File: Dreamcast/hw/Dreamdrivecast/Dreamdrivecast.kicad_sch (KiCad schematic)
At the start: 9 parts, among them CN1 Molex_52602_0579, J1 Breakout, J2 POWER, J4 Micro_SD_Card, SW1 Lid, U1 WeAct-RP2040-Pico, U2 WeAct-RP2040-Pico

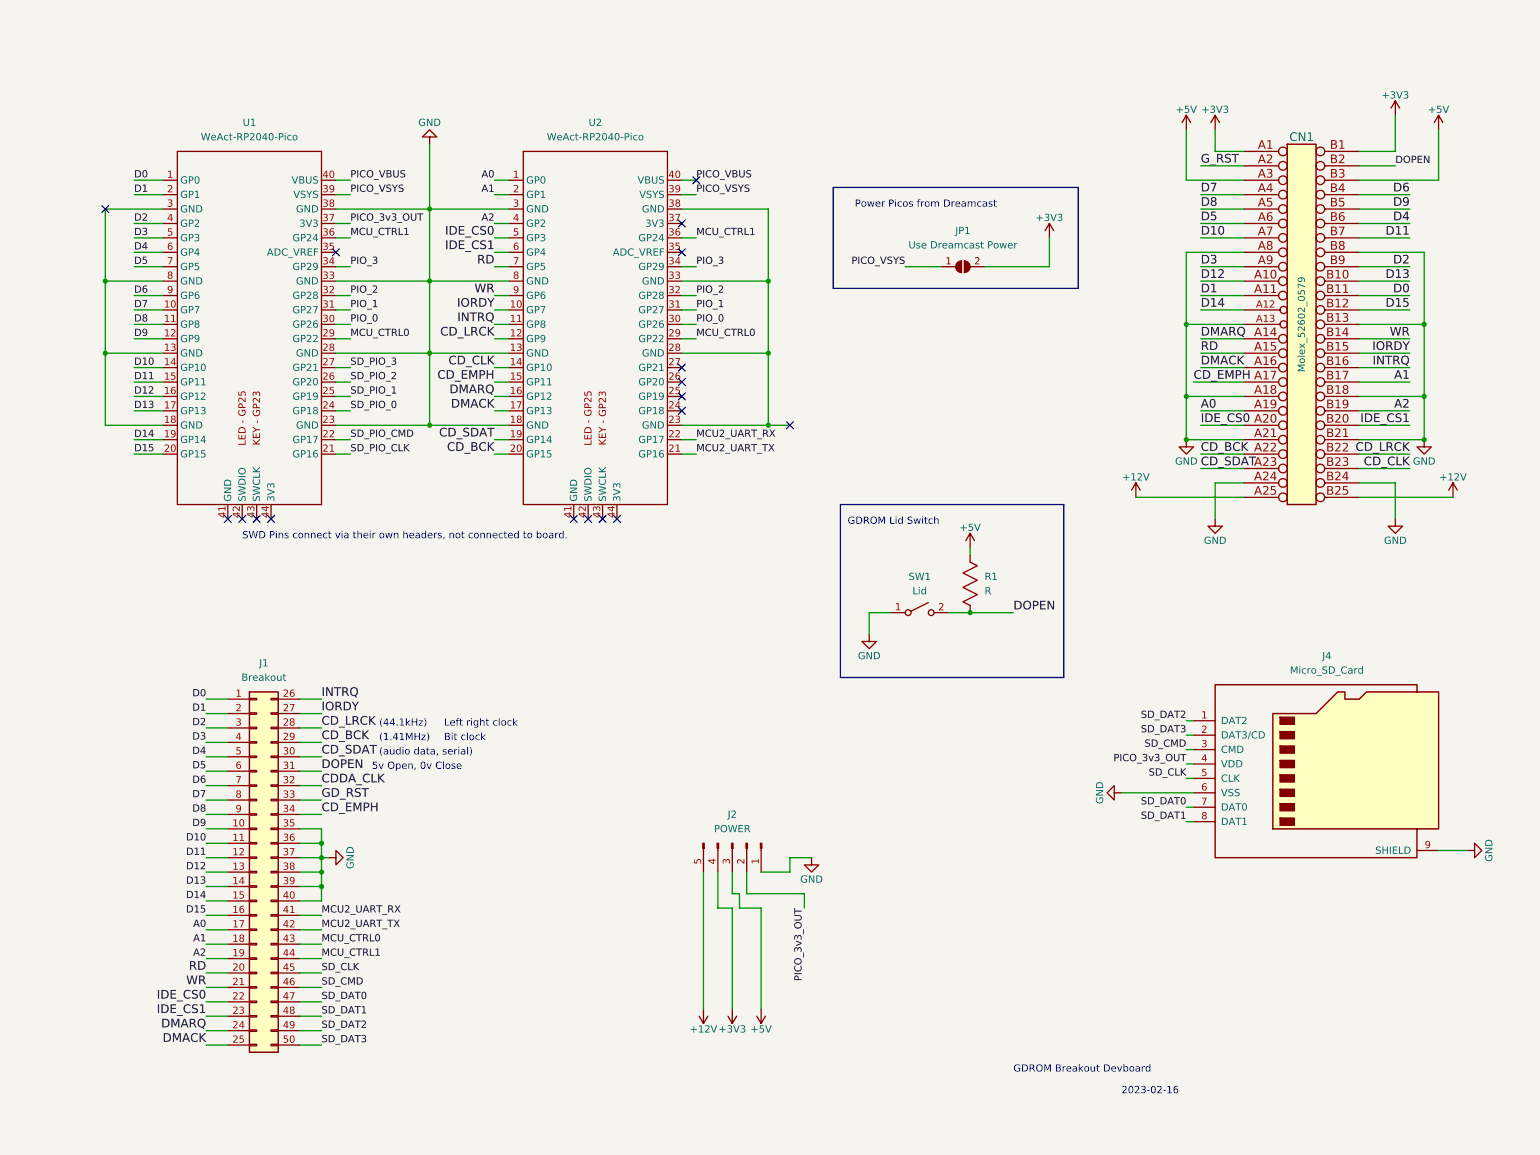
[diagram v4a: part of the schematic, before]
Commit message: Routed board, did copper fill, added silk screen for breakout, added logo and board text. Ready for fab
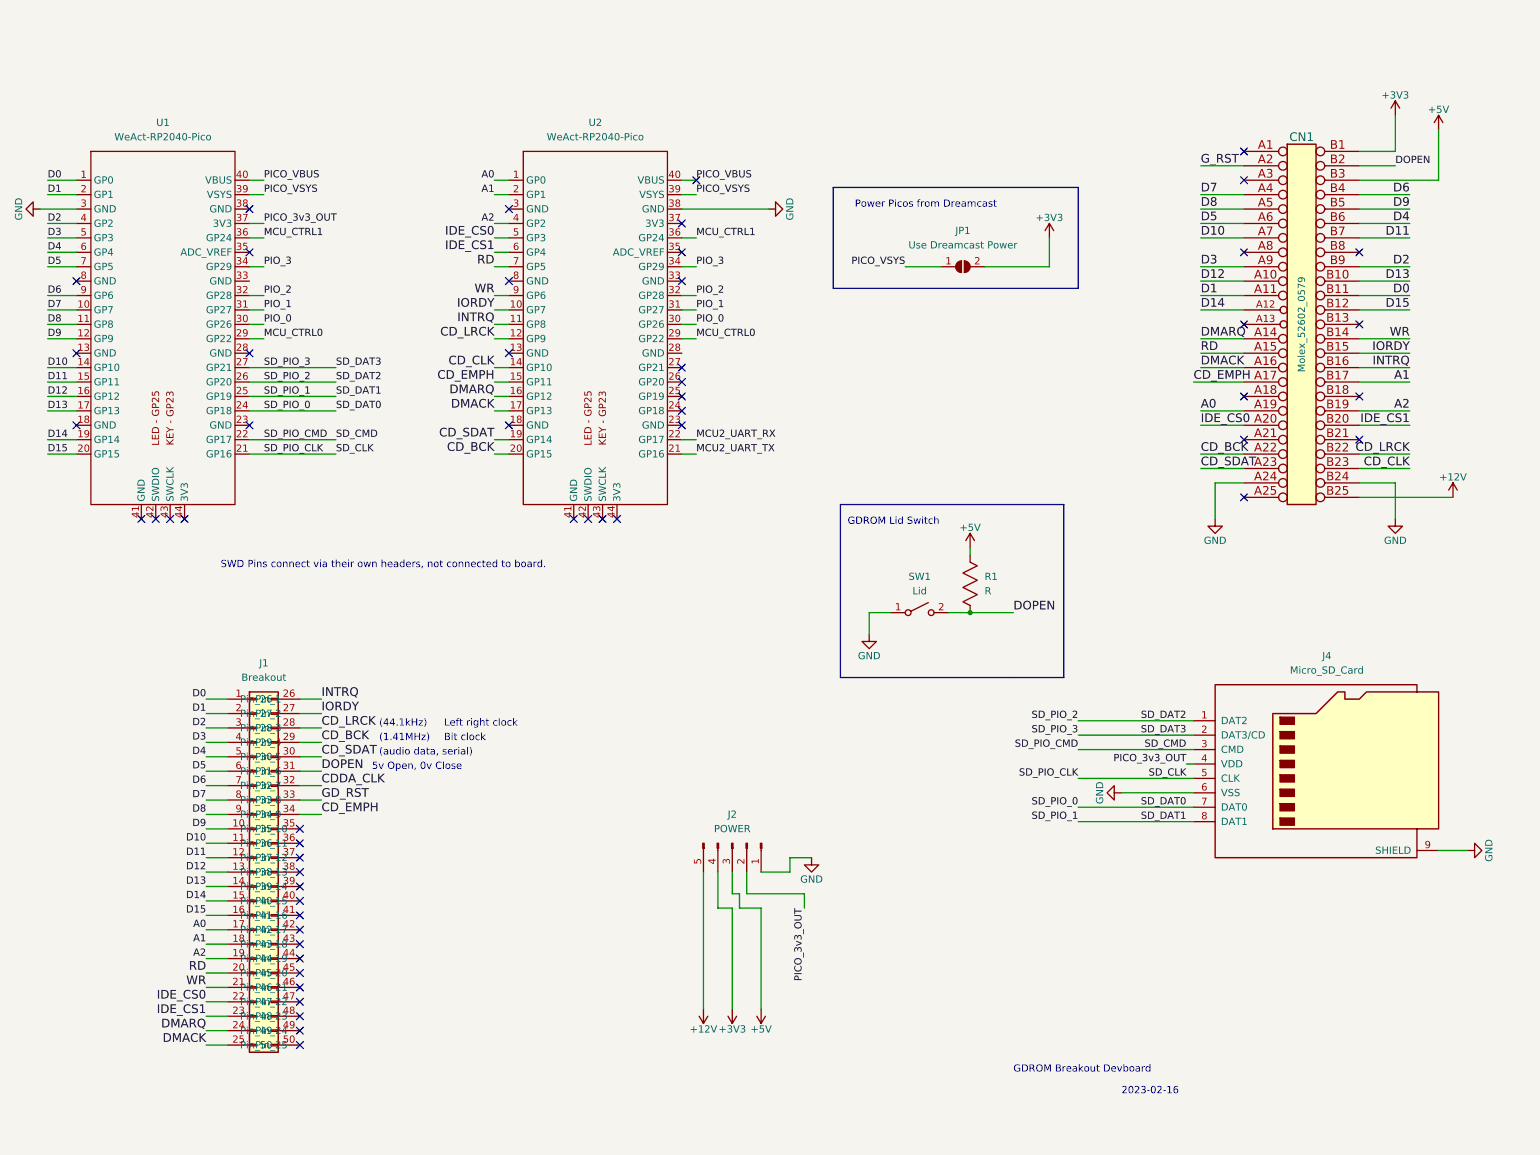
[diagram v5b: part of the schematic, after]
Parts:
- J1: footprint Connector_PinHeader_2.54mm:PinHeader_2x25_P2.54mm_Vertical_SMD -> Connector_PinHeader_2.54mm:PinHeader_2x20_P2.54mm_Vertical_SMD
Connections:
- net SD_PIO_0 is gone; now on net SD_DAT0: U1.24 (GP18)
- net SD_PIO_1 is gone; now on net SD_DAT1: U1.25 (GP19)
- net SD_PIO_2 is gone; now on net SD_DAT2: U1.26 (GP20)
- net SD_PIO_3 is gone; now on net SD_DAT3: U1.27 (GP21)
- net SD_PIO_CLK is gone; now on net SD_CLK: U1.21 (GP16)
- net SD_PIO_CMD is gone; now on net SD_CMD: U1.22 (GP17)
- net +12V: no longer CN1.A25
- net +3V3: no longer CN1.A1
- net +5V: no longer CN1.A3
- net GND: now also U1.3 (GND), U2.38 (GND); no longer CN1.A13, CN1.A18, CN1.A21, CN1.A8, CN1.B13, CN1.B18, CN1.B21, CN1.B8, J1.35 (Pin_35), J1.36 (Pin_36), J1.37 (Pin_37), J1.38 (Pin_38), J1.39 (Pin_39), J1.40 (Pin_40), U1.23 (GND), U1.28 (GND), U1.33 (GND), U1.38 (GND), U2.13 (GND), U2.18 (GND), U2.3 (GND), U2.8 (GND)
- net MCU2_UART_RX: no longer J1.41 (Pin_41)
- net MCU2_UART_TX: no longer J1.42 (Pin_42)
- net MCU_CTRL0: no longer J1.43 (Pin_43)
- net MCU_CTRL1: no longer J1.44 (Pin_44)
- net SD_CLK: no longer J1.45 (Pin_45)
- net SD_CMD: no longer J1.46 (Pin_46)
- net SD_DAT0: no longer J1.47 (Pin_47)
- net SD_DAT1: no longer J1.48 (Pin_48)
- net SD_DAT2: no longer J1.49 (Pin_49)
- net SD_DAT3: no longer J1.50 (Pin_50)
- now unconnected: U1.13 (GND), U1.18 (GND), U1.8 (GND), U2.23 (GND), U2.28 (GND), U2.33 (GND)
- no-connect marks 18 -> 55
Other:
- moved on the sheet: U1

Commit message: Update schematic to use rp2040s, mux the control lines with some data pins on mcu1, and change the pinout. PCB hasn't been rerouted yet.
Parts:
- removed J2: POWER, Connector_PinHeader_2.54mm:PinHeader_1x05_P2.54mm_Vertical, symbol Connector:Conn_01x05_Male
- removed U1, U2: WeAct-RP2040-Pico, WeAct-RP2040-Pico:WeAct-RP2040-Pico, symbol Weact-RP2040-Pico:WeAct-RP2040-Pico
- added C1, C14, C15, C16, C17, C18, C19, C2, C3, C4, C5, C6: 100n, Capacitor_SMD:C_0402_1005Metric, symbol Device:C
- added C10, C22, C23, C9: 1u, Capacitor_SMD:C_0402_1005Metric, symbol Device:C
- added C11, C12: 10u, Capacitor_SMD:C_0603_1608Metric, symbol Device:C_Small
- added C13, C24: 100n, Capacitor_SMD:C_0603_1608Metric, symbol Device:C_Small
- added C20, C21, C8: C, Capacitor_SMD:C_0402_1005Metric, symbol Device:C
- added C7: C, symbol Device:C
- added C? (x4): 12p, Capacitor_SMD:C_0402_1005Metric, symbol Device:C_Small
- added J2, J5: USB_C_Receptacle_USB2.0, Connector_USB_Extra:USB_C_Receptacle_GT-USB-7010, symbol Connector:USB_C_Receptacle_USB2.0
- added J3: POWER, Connector_PinHeader_2.54mm:PinHeader_1x05_P2.54mm_Vertical, symbol Connector:Conn_01x05_Male
- added R10, R2, R3, R9: 27.4, Resistor_SMD:R_0402_1005Metric, symbol Device:R
- added R11, R12, R4, R5: 5k1, Resistor_SMD:R_0402_1005Metric, symbol Device:R_Small
- added R13, R8: 100k, Resistor_SMD:R_0402_1005Metric, symbol Device:R_Small
- added R14, R6: 10k, Resistor_SMD:R_0402_1005Metric, symbol Device:R
- added R15, R7: 1k, Resistor_SMD:R_0402_1005Metric, symbol Device:R
- added SW2: MCU1_BOOT, symbol Switch:SW_Push
- added SW3: MCU2_BOOT, symbol Switch:SW_Push
- added U1: TS3L501ERUA, Package_DFN_QFN:WQFN-42-1EP_3.5x9mm_P0.5mm_EP2.05x7.55mm, symbol Analog_Switch:TS3L501ERUA
- added U2, U5: RP2040, Package_DFN_QFN:QFN-56-1EP_7x7mm_P0.4mm_EP3.2x3.2mm, symbol MCU_RaspberryPi:RP2040
- added U3: AZ1117-3.3, Package_TO_SOT_SMD:SOT-223, symbol Regulator_Linear:AZ1117-3.3
- added U4, U6: W25Q128JVS, Package_SO:SOIC-8_5.23x5.23mm_P1.27mm, symbol Memory_Flash:W25Q128JVS
- added Y? (x2): 12MHz 10ppm, Crystal:Crystal_SMD_2520-4Pin_2.5x2.0mm, symbol Device:Crystal_GND24_Small
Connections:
- net +12V: now also CN1.A25, J3.5 (Pin_5)
- net +3V3: now also C1.1, C10.1, C12.1, C13.1, C14.1, C15.1, C16.1, C17.1, C18.1, C19.1, C2.1, C23.1, C24.1, C3.1, C4.1, C5.1, C6.1, J3.4 (Pin_4), R14.1, R6.1, U1.1 (VDD), U1.14 (VDD), U1.21 (VDD), U1.30 (VDD), U1.39 (VDD), U1.4 (VDD), U1.8 (VDD), U2.1 (IOVDD), U2.10 (IOVDD), U2.22 (IOVDD), U2.33 (IOVDD), U2.42 (IOVDD), U2.43 (ADC_AVDD), U2.44 (VREG_IN), U2.48 (USB_VDD), U2.49 (IOVDD), U3.2 (VO), U4.8 (VCC), U5.1 (IOVDD), U5.10 (IOVDD), U5.22 (IOVDD), U5.33 (IOVDD), U5.42 (IOVDD), U5.43 (ADC_AVDD), U5.44 (VREG_IN), U5.48 (USB_VDD), U5.49 (IOVDD), U6.8 (VCC); no longer CN1.B1, JP1.2 (B)
- net +5V: now also CN1.A3, J3.3 (Pin_3)
- net A0: now also U1.38 (B0)
- net A1: now also U1.37 (B1)
- net A2: now also U1.34 (B2)
- net CD_BCK: now also U5.4 (GPIO2)
- net CD_CLK: now also U5.2 (GPIO0)
- net CD_EMPH: now also U5.6 (GPIO4)
- net CD_LRCK: now also U5.3 (GPIO1)
- net CD_SDAT: now also U5.5 (GPIO3)
- net D0: now also U1.36 (C0)
- net D1: now also U1.35 (C1)
- net D10: now also U2.13 (GPIO10)
- net D11: now also U2.14 (GPIO11)
- net D12: now also U2.15 (GPIO12)
- net D13: now also U2.16 (GPIO13)
- net D14: now also U2.17 (GPIO14)
- net D15: now also U2.18 (GPIO15)
- net D2: now also U1.32 (C2)
- net D3: now also U1.31 (C3)
- net D4: now also U1.27 (C4)
- net D5: now also U2.7 (GPIO5)
- net D6: now also U2.8 (GPIO6)
- net D7: now also U2.9 (GPIO7)
- net D8: now also U2.11 (GPIO8)
- net D9: now also U2.12 (GPIO9)
- net DMACK: now also U2.30 (GPIO19)
- net DMARQ: now also U2.31 (GPIO20)
- net GND: now also CN1.A13, CN1.A18, CN1.A21, CN1.A8, CN1.B13, CN1.B18, CN1.B21, CN1.B8, C1.2, C10.2, C11.2, C12.2, C13.2, C14.2, C15.2, C16.2, C17.2, C18.2, C19.2, C2.2, C20.2, C21.2, C22.2, C23.2, C24.2, C3.2, C4.2, C5.2, C6.2, C7.2, C8.2, C9.2, C?.1, C?.1, C?.1, C?.1, J2.A1 (GND), J2.A12 (GND), J2.B1 (GND), J2.B12 (GND), J3.1 (Pin_1), J5.A1 (GND), J5.A12 (GND), J5.B1 (GND), J5.B12 (GND), R11.2, R12.2, R13.1, R4.2, R5.2, R8.1, SW2.1, SW3.1, U1.43 (GND), U1.5 (PD), U2.19 (TESTEN), U2.57 (GND), U3.1 (GND), U4.4 (GND), U5.19 (TESTEN), U5.57 (GND), U6.4 (GND), Y?.2, Y?.2, Y?.4, Y?.4
- net INTRQ: now also U2.29 (GPIO18)
- net IORDY: now also U5.18 (GPIO15)
- net PICO_3v3_OUT: now also J3.2 (Pin_2)
- net +3V3_DREAMCAST: now reaches CN1.A1
- net +3V3_DREAMCAST: now also CN1.B1, JP1.2 (B)
- net RD renamed MCU1_GPIO16
- net MCU1_GPIO16: now also U2.27 (GPIO16)
- net SD_CLK renamed MCU1_GPIO21
- net MCU1_GPIO21: now also U2.32 (GPIO21)
- net SD_CMD renamed MCU1_GPIO22
- net MCU1_GPIO22: now also U2.34 (GPIO22)
- net SD_DAT0 renamed MCU1_GPIO23
- net MCU1_GPIO23: now also U2.35 (GPIO23)
- net SD_DAT1 renamed MCU1_GPIO24
- net MCU1_GPIO24: now also U2.36 (GPIO24)
- net SD_DAT2 renamed MCU1_GPIO25
- net MCU1_GPIO25: now also U2.37 (GPIO25)
- net SD_DAT3 renamed MCU1_GPIO26
- net MCU1_GPIO26: now also U2.38 (GPIO26_ADC0)
- net WR renamed MCU1_GPIO17
- net MCU1_GPIO17: now also U2.28 (GPIO17)
- new net: J2.B5 (CC2), R5.1
- new net: R2.2, U2.47 (USB_DP)
- new net: J5.A4 (VBUS), J5.A9 (VBUS), J5.B4 (VBUS), J5.B9 (VBUS)
- new net: J5.A5 (CC1), R11.1
- new net: J5.B5 (CC2), R12.1
- new net: J5.S1 (SHIELD), R13.2
- new net: R3.2, U2.46 (USB_DM)
- new net: J2.A5 (CC1), R4.1
- new net: R7.1, SW2.2
- new net: J2.S1 (SHIELD), R8.2
- new net: R15.1, SW3.2
- new net: R10.2, U5.46 (USB_DM)
- new net: R9.2, U5.47 (USB_DP)
- new net +1V1: C20.1, C21.1, C22.1, C7.1, C8.1, C9.1, U2.23 (DVDD), U2.45 (VREG_VOUT), U2.50 (DVDD), U5.23 (DVDD), U5.45 (VREG_VOUT), U5.50 (DVDD)
- new net COMMS_PIO_0: U2.40 (GPIO28_ADC2), U5.7 (GPIO5)
- new net COMMS_PIO_1: U2.41 (GPIO29_ADC3), U5.8 (GPIO6)
- new net CS0: U1.33 (B3)
- new net CS1: U1.29 (B4)
- new net MCU1_GPIO0: U1.2 (A0), U2.2 (GPIO0)
- new net MCU1_GPIO1: U1.3 (A1), U2.3 (GPIO1)
- new net MCU1_GPIO2: U1.6 (A2), U2.4 (GPIO2)
- new net MCU1_GPIO27: U1.13 (SEL), U2.39 (GPIO27_ADC1)
- new net MCU1_GPIO3: U1.7 (A3), U2.5 (GPIO3)
- new net MCU1_GPIO4: U1.9 (A4), U2.6 (GPIO4)
- new net MCU1_QSPI_SCLK: U2.52 (QSPI_SCLK), U4.6 (CLK)
- new net MCU1_QSPI_SD0: U2.53 (QSPI_SD0), U4.5 (DI(IO0))
- new net MCU1_QSPI_SD1: U2.55 (QSPI_SD1), U4.2 (DO(IO1))
- new net MCU1_QSPI_SD2: U2.54 (QSPI_SD2), U4.3 (IO2)
- new net MCU1_QSPI_SD3: U2.51 (QSPI_SD3), U4.7 (IO3)
- new net MCU1_QSPI_SS: R6.2, R7.2, U2.56 (QSPI_SS), U4.1 (~{CS})
- new net MCU1_RUN: U2.26 (RUN), U5.26 (RUN)
- new net MCU1_SWCLK: U2.24 (SWCLK)
- new net MCU1_SWD: U2.25 (SWD)
- new net MCU1_USB_D+: J2.A6 (D+), J2.B6 (D+), R2.1
- new net MCU1_USB_D-: J2.A7 (D-), J2.B7 (D-), R3.1
- new net MCU1_XIN: C?.2, U2.20 (XIN), Y?.3
- new net MCU1_XOUT: C?.2, U2.21 (XOUT), Y?.1
- new net MCU2_GPIO10: U5.13 (GPIO10)
- new net MCU2_GPIO11: U5.14 (GPIO11)
- new net MCU2_GPIO12: U5.15 (GPIO12)
- new net MCU2_GPIO13: U5.16 (GPIO13)
- new net MCU2_GPIO14: U5.17 (GPIO14)
- new net MCU2_GPIO16: U5.27 (GPIO16)
- new net MCU2_GPIO17: U5.28 (GPIO17)
- new net MCU2_GPIO18: U5.29 (GPIO18)
- new net MCU2_GPIO19: U5.30 (GPIO19)
- new net MCU2_GPIO20: U5.31 (GPIO20)
- new net MCU2_GPIO21: U5.32 (GPIO21)
- new net MCU2_GPIO22: U5.34 (GPIO22)
- new net MCU2_GPIO23: U5.35 (GPIO23)
- new net MCU2_GPIO24: U5.36 (GPIO24)
- new net MCU2_GPIO25: U5.37 (GPIO25)
- new net MCU2_GPIO26: U5.38 (GPIO26_ADC0)
- new net MCU2_GPIO27: U5.39 (GPIO27_ADC1)
- new net MCU2_GPIO28: U5.40 (GPIO28_ADC2)
- new net MCU2_GPIO29: U5.41 (GPIO29_ADC3)
- new net MCU2_GPIO7: U5.9 (GPIO7)
- new net MCU2_GPIO8: U5.11 (GPIO8)
- new net MCU2_GPIO9: U5.12 (GPIO9)
- new net MCU2_QSPI_SCLK: U5.52 (QSPI_SCLK), U6.6 (CLK)
- new net MCU2_QSPI_SD0: U5.53 (QSPI_SD0), U6.5 (DI(IO0))
- new net MCU2_QSPI_SD1: U5.55 (QSPI_SD1), U6.2 (DO(IO1))
- new net MCU2_QSPI_SD2: U5.54 (QSPI_SD2), U6.3 (IO2)
- new net MCU2_QSPI_SD3: U5.51 (QSPI_SD3), U6.7 (IO3)
- new net MCU2_QSPI_SS: R14.2, R15.2, U5.56 (QSPI_SS), U6.1 (~{CS})
- new net MCU2_SWCLK: U5.24 (SWCLK)
- new net MCU2_SWD: U5.25 (SWD)
- new net MCU2_USB_D+: J5.A6 (D+), J5.B6 (D+), R9.1
- new net MCU2_USB_D-: J5.A7 (D-), J5.B7 (D-), R10.1
- new net MCU2_XIN: C?.2, U5.20 (XIN), Y?.3
- new net MCU2_XOUT: C?.2, U5.21 (XOUT), Y?.1
- new net MUX_B_5: U1.28 (B5)
- new net MUX_B_6: U1.25 (B6)
- new net MUX_B_7: U1.24 (B7)
- new net MUX_COMMON_5: U1.10 (A5)
- new net MUX_COMMON_6: U1.11 (A6)
- new net MUX_COMMON_7: U1.12 (A7)
- new net MUX_C_5: U1.26 (C5)
- new net MUX_C_6: U1.23 (C6)
- new net MUX_C_7: U1.22 (C7)
- new net VBUS: C11.1, J2.A4 (VBUS), J2.A9 (VBUS), J2.B4 (VBUS), J2.B9 (VBUS), U3.3 (VI)
- no-connect marks 55 -> 29
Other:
- note added: "2023-04-20"
- note added: "AICA Chip Clock"
- note added: "Asserted in PIO mode, Deasserted in DMA mode"
- note added: "Breakouts"
- note added: "Crystals"
- note added: "DREAMCAST"
- note added: "GDROM DEV BOARD"
- note added: "IORDY - Used to signal to host that device needs more time"
- note added: "MCU1"
- note added: "MCU1 Connections"
- note added: "MCU1 Flash"
- note added: "MCU1 MUX"
- note added: "MCU1 USB connector"
- note added: "MCU2"
- note added: "MCU2 Connections"
- note added: "MCU2 Flash"
- note added: "MCU2 USB connector"
- note added: "Reset the GDROM Drive?"
- note added: "SD Card"
- note added: "USE MCU1's POWER???"
- note added: "Unused for the moment"
- note removed: "2023-02-16"
- note removed: "GDROM Breakout Devboard"
- note removed: "SWD Pins connect via their own headers, not connected to board."
- moved on the sheet: CN1, J1, J4, JP1, R1, SW1

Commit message: Updated PCB for new schematic design, still needs to be routed.
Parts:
- C11, C12, C13, C24: footprint Capacitor_SMD:C_0603_1608Metric -> Capacitor_SMD:C_0402_1005Metric
- C20, C21, C7, C8: value C -> 100n
- J1: now left out of the parts list
- J3: renamed from J2; footprint Connector_USB_Extra:USB_C_Receptacle_GT-USB-7010 -> Connector_USB:USB_C_Receptacle_Palconn_UTC16-G
- J4: renamed from J5; footprint Connector_USB_Extra:USB_C_Receptacle_GT-USB-7010 -> Connector_USB:USB_C_Receptacle_Palconn_UTC16-G
- SW2, SW3: footprint (none) -> Button_Switch_SMD:SW_SPST_FSMSM
- gave numbers to parts that had none: 6
- renumbered J3 to J2, J4 to J5
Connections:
- net PICO_VSYS is gone; now on net VBUS: JP1.1 (A)
- net MCU1_RUN: no longer U5.26 (RUN)
- net MCU1_XIN: now also C25.2, Y1.3; no longer C26.2, Y2.3
- net MCU1_XOUT: now also C27.2, Y1.1; no longer C28.2, Y2.1
- net MCU2_XIN: now also C26.2, Y2.3; no longer C25.2, Y1.3
- net MCU2_XOUT: now also C28.2, Y2.1; no longer C27.2, Y1.1
- new net MCU2_RUN: U5.26 (RUN)

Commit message: Updated pcb for new schematic.
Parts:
- C7: footprint (none) -> Capacitor_SMD:C_0402_1005Metric
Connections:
- net CS0: now also CN1.A20
- net CS1: now also CN1.B20
- net IDE_CS0: no longer CN1.A20
- net IDE_CS1: no longer CN1.B20
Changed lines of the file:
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@@
     (effects (font (size 1.524 1.524)) (justify right bottom))
   )
-  (label "IDE_CS0" (at 488.95 186.69 0)
+  (label "CS0" (at 488.95 186.69 0)
     (effects (font (size 1.524 1.524)) (justify left bottom))
   )
@@
     (effects (font (size 1.27 1.27)) (justify left bottom))
   )
-  (label "IDE_CS1" (at 525.78 186.69 180)
+  (label "CS1" (at 525.78 186.69 180)
     (effects (font (size 1.524 1.524)) (justify right bottom))
   )
@@
       (effects (font (size 1.27 1.27)) (justify left))
     )
-    (property "Footprint" "" (id 2) (at 67.0052 38.1 0)
-      (effects (font (size 1.27 1.27)) hide)
-    )
+    (property "Footprint" "Capacitor_SMD:C_0402_1005Metric" (id 2) (at 67.0052 38.1 0)
+      (effects (font (size 1.27 1.27)) hide)
+    )
